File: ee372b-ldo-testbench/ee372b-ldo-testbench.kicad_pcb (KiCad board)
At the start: 4 copper layers, 118 parts, among them J1 PEC02SAAN, J10 OUT_S, J11 VOUT, J12 VDD_BUF, J13 V_SIG, J14 PEC03SAAN, J15 VSIG_BUF, J16 PEC03SAAN, J17 PEC03SAAN, J18 PEC03SAAN, J19 PEC03SAAN, J2 PEC02SAAN, J20 VREF_EXTERNAL, J21 PEC02SAAN, J22 PEC02SAAN, J23 PEC02SAAN, J24 PEC02SAAN, J25 PEC03SAAN, J3 GND, J4 1V8, J5 3v3_EXTERNAL, J9 IN_S, Q1 FDV305N, Q2 FDV305N, Q3 FDV305N, Q4 FDV305N, Q5 FDV305N, U1 MMSZ4679T1G, U3 ADS1220IPW, U4 BUF634AIDR

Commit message: omg fit everything in 100x100
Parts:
- added R64: 0, Resistor_SMD:R_0805_2012Metric_Pad1.20x1.40mm_HandSolder, F.Cu at (169.8, 50.4)
- added R65: 0, Resistor_SMD:R_0805_2012Metric_Pad1.20x1.40mm_HandSolder, F.Cu at (172.8, 50.4)
- moved C16 96.8 mm to (162.7, 68.1), turned to -90 degrees
- moved C14 96.5 mm to (173.4, 68.2), turned to -90 degrees
- moved C15 96.5 mm to (168.0, 68.1), turned to -90 degrees
- moved C2 88.7 mm to (175.7, 58.2)
- moved C1 88.7 mm to (175.7, 62.1)
- moved C8 88.7 mm to (177.7, 58.2)
- moved C12 88.7 mm to (177.7, 62.1)
- moved J25 88.2 mm to (162.1, 49.5), turned to -90 degrees
- moved U3 87.4 mm to (169.7, 61.2)
- moved R6 86.4 mm to (175.5, 68.2), turned to 90 degrees
- moved R1 85.2 mm to (162.9, 60.5)
- moved R2 85.2 mm to (162.9, 58.4)
- moved R5 84.9 mm to (181.8, 57.3), turned to 180 degrees
- moved R44 83.7 mm to (166.6, 50.4)
- moved R8 83.5 mm to (164.8, 68.2), turned to 90 degrees
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
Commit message: re add caps for each pin
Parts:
- removed C27: 100nF, Capacitor_SMD:C_0805_2012Metric_Pad1.18x1.45mm_HandSolder
- added C24: 100nF, Capacitor_SMD:C_0805_2012Metric_Pad1.18x1.45mm_HandSolder, F.Cu at (198.7, 37.3)
- added C29: 100nF, Capacitor_SMD:C_0805_2012Metric_Pad1.18x1.45mm_HandSolder, F.Cu at (201.4, 49.3)
- added C30: 100nF, Capacitor_SMD:C_0805_2012Metric_Pad1.18x1.45mm_HandSolder, F.Cu at (206.9, 40.1)
- moved J3 15.1 mm to (145.2, 76.7)
- moved J5 15.0 mm to (145.2, 91.8)
- moved R37 1.74 mm to (202.9, 24.1)
- moved R48 1.29 mm to (199.8, 56.6)
- moved R49 1.29 mm to (207.3, 56.6)
- moved R58 1.29 mm to (204.8, 56.6)
- moved R60 1.29 mm to (201.8, 56.6)
- moved C7 1.14 mm to (203.5, 49.3)
- moved J25 0.15 mm to (162.2, 49.6)
- turned C23 to -90 degrees
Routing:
- net Net-(C10-Pad2): track 0.00 -> 1.48 mm

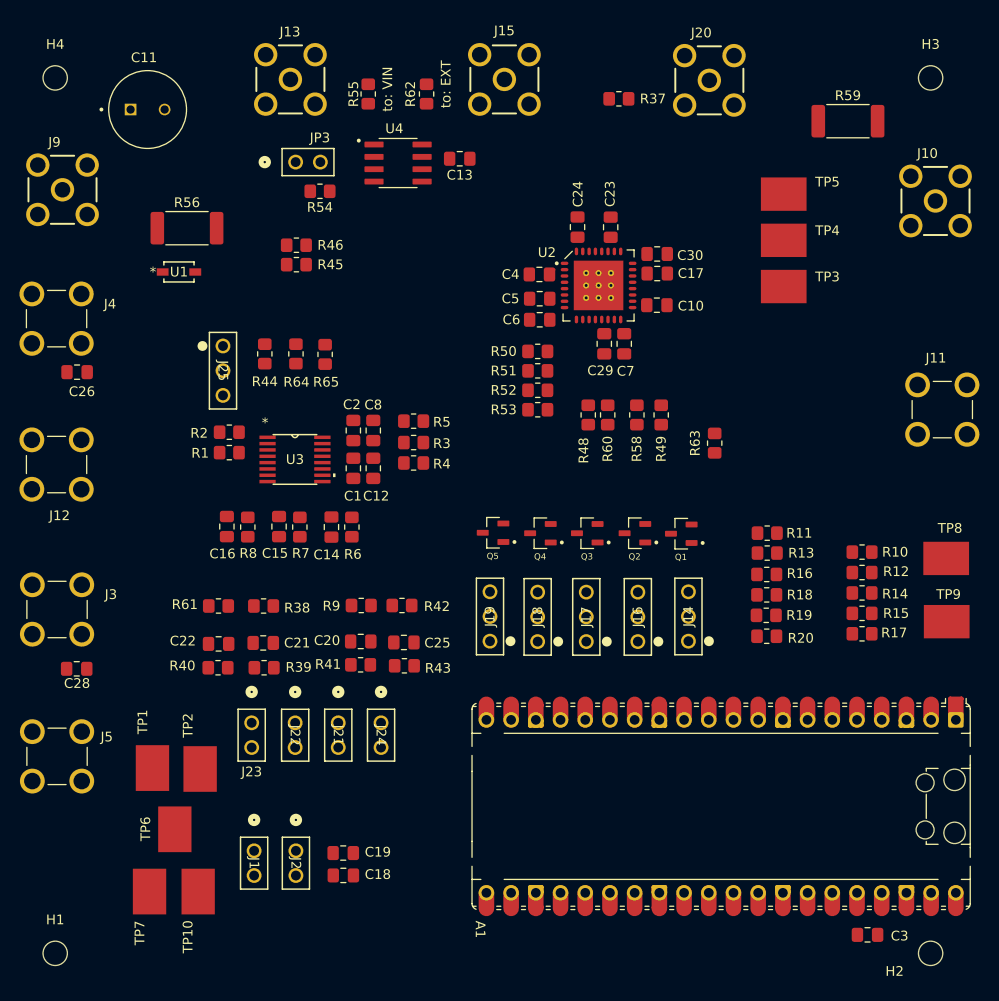
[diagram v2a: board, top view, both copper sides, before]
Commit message: added more GND test points and EP to VSS r0 thing
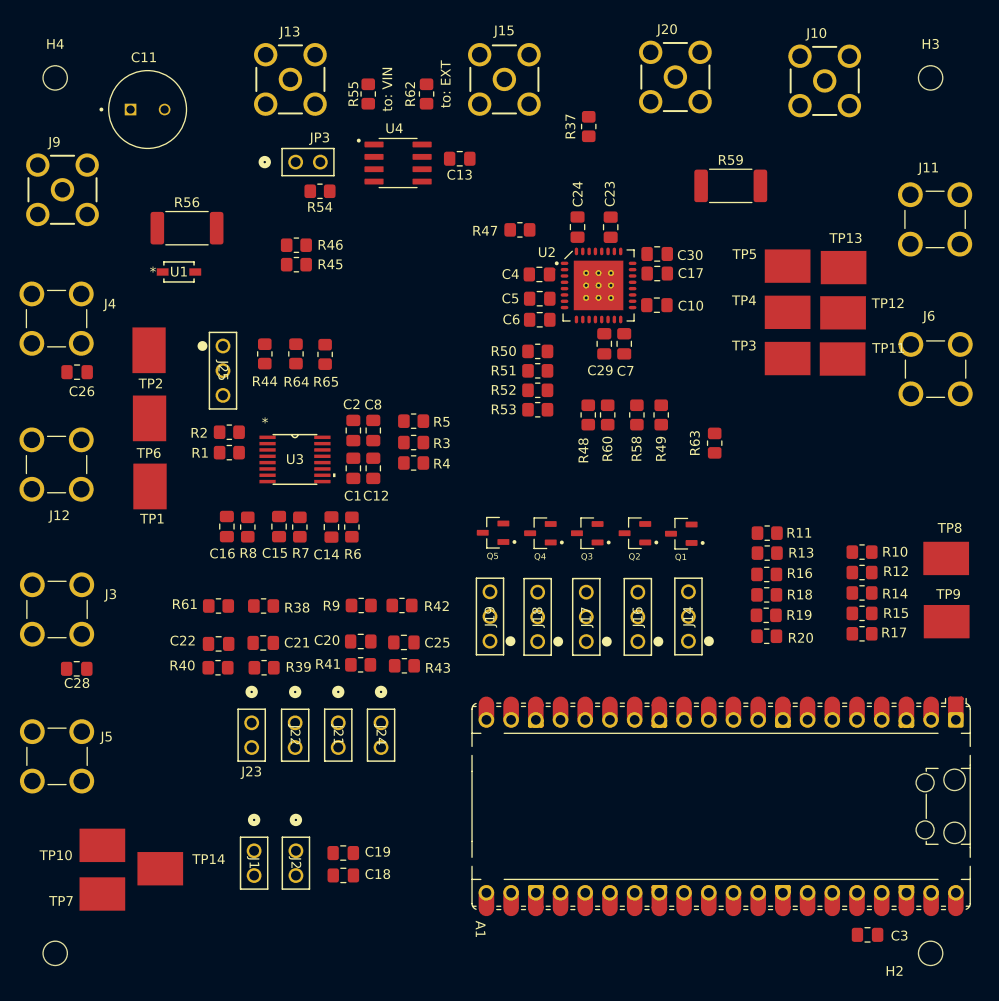
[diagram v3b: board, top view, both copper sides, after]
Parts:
- added J6: GND, 1_EE372_DemoBoard:CALTEST_CT3151-2, F.Cu at (235.5, 51.9)
- added R47: 0, Resistor_SMD:R_0805_2012Metric_Pad1.20x1.40mm_HandSolder, F.Cu at (192.8, 37.6)
- added TP11: GND, 1_EE372_DemoBoard:KEYSTONE_5016, F.Cu at (225.9, 50.9)
- added TP12: GND, 1_EE372_DemoBoard:KEYSTONE_5016, F.Cu at (226.0, 46.1)
- added TP13: GND, 1_EE372_DemoBoard:KEYSTONE_5016, F.Cu at (226.1, 41.5)
- added TP14: GND, 1_EE372_DemoBoard:KEYSTONE_5016, F.Cu at (155.8, 103.3)
- moved TP2 43.4 mm to (154.7, 50.0), turned to -90 degrees
- moved TP6 42.3 mm to (154.7, 57.0), turned to -90 degrees
- moved TP1 29.0 mm to (154.8, 64.0), turned to -90 degrees
- moved J11 19.6 mm to (235.5, 36.5)
- moved J10 16.8 mm to (224.1, 22.3)
- moved R59 13.8 mm to (214.4, 33.1)
- moved TP10 10.9 mm to (149.8, 100.9), turned to 180 degrees
- moved TP3 7.41 mm to (220.3, 50.9)
- moved TP4 7.41 mm to (220.3, 46.1)
- moved TP5 7.41 mm to (220.3, 41.4)
- moved TP7 4.86 mm to (149.8, 105.9), turned to 180 degrees
- moved R37 4.21 mm to (199.8, 27.0), turned to -90 degrees
- moved J20 3.51 mm to (208.8, 21.9)
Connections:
- U2 pad 33: unconnected-(U2-EP-Pad33)_8 -> Net-(U2-EP)

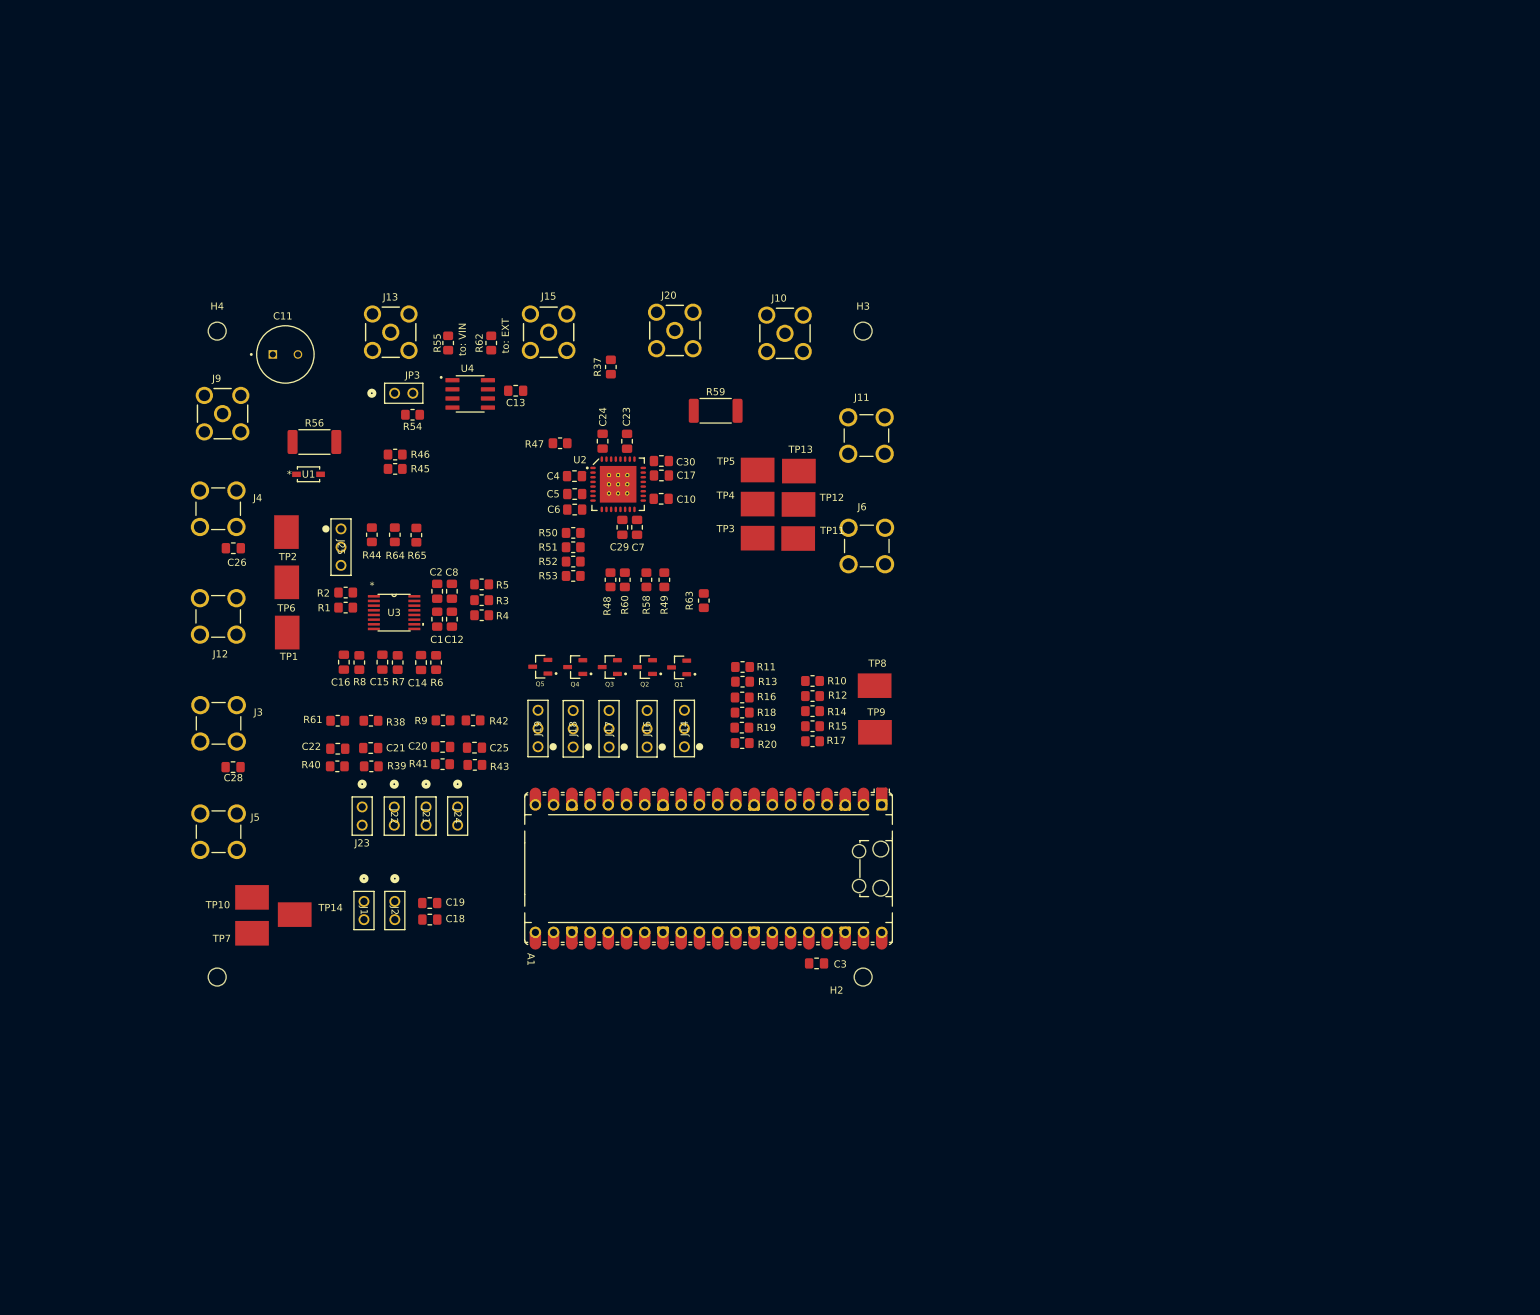
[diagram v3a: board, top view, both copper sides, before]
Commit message: first plane fill on L2 GND
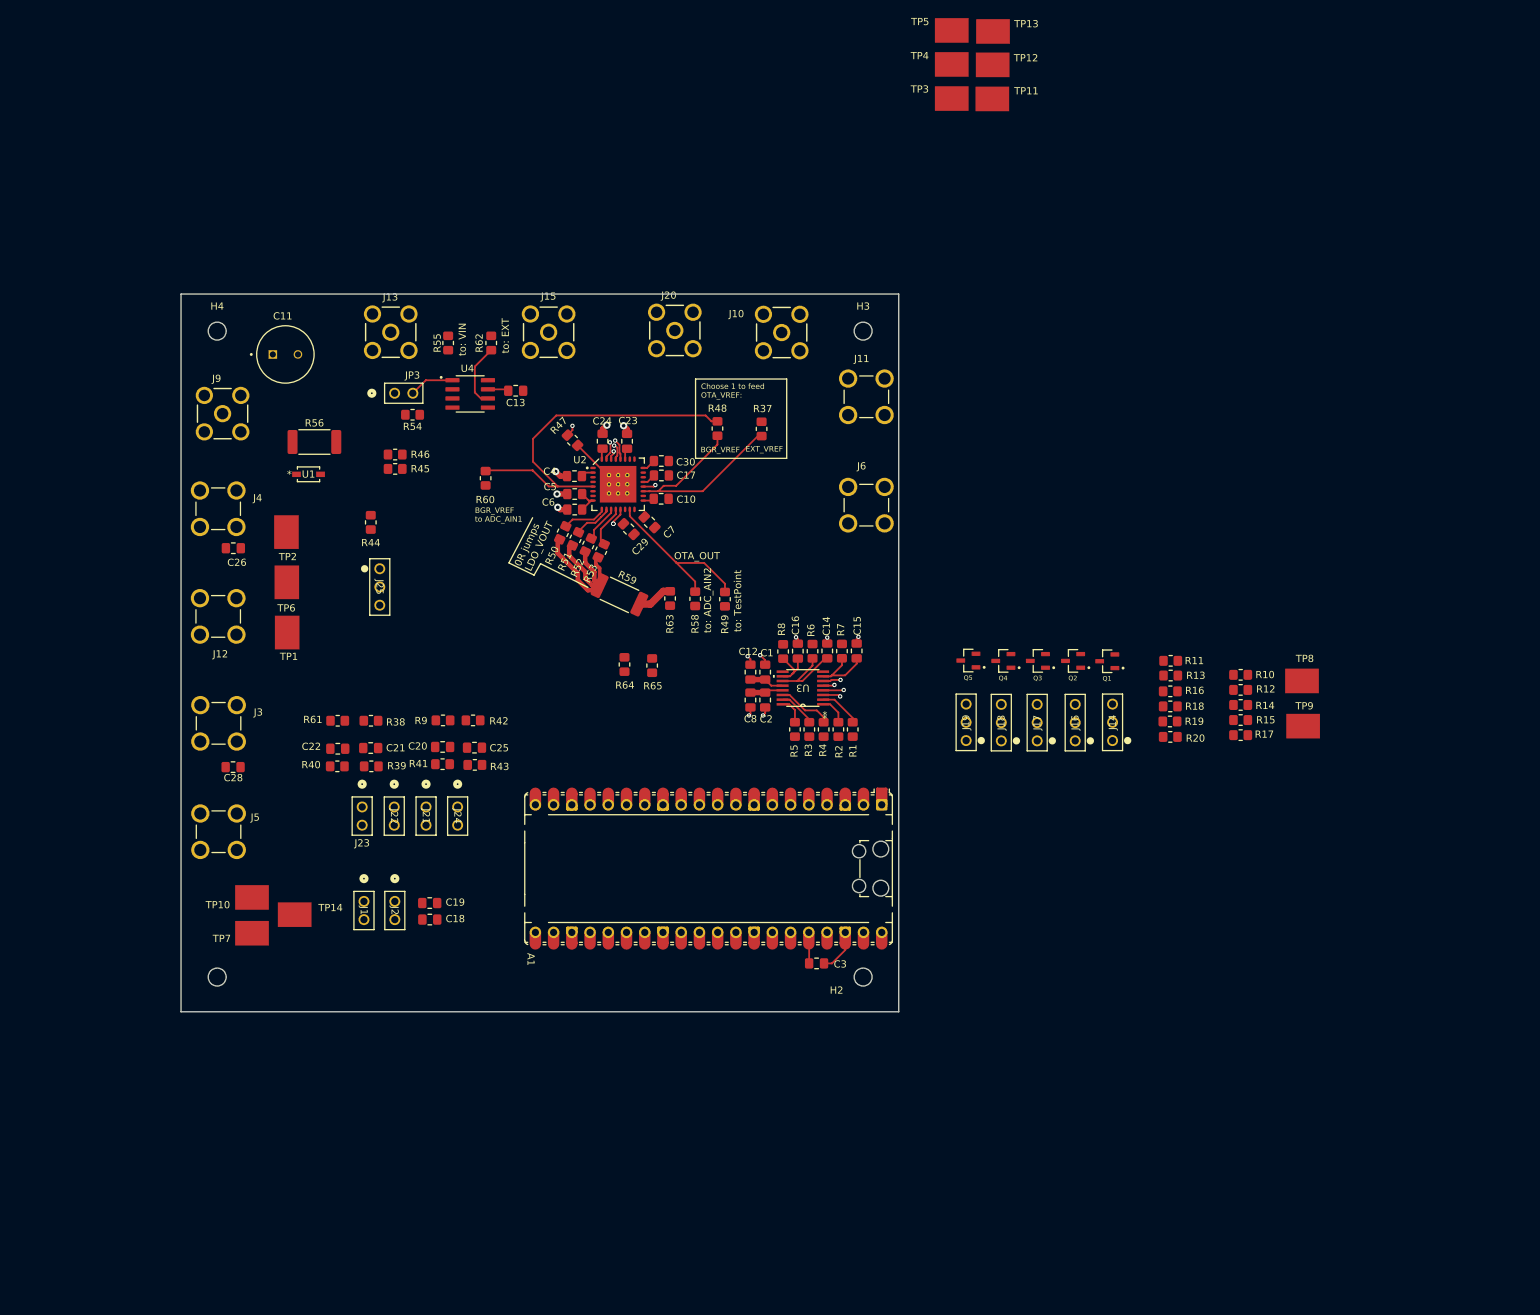
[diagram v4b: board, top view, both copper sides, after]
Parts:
- moved R1 72.7 mm to (233.6, 77.5), turned to -90 degrees
- moved R2 71.3 mm to (231.6, 77.5), turned to 90 degrees
- moved TP11 67.0 mm to (253.0, -10.3)
- moved TP12 67.0 mm to (253.1, -15.1)
- moved TP13 67.0 mm to (253.1, -19.8)
- moved TP3 67.0 mm to (247.3, -10.4)
- moved TP4 67.0 mm to (247.3, -15.2)
- moved TP5 67.0 mm to (247.3, -19.9)
- moved C15 66.1 mm to (234.1, 66.6), turned to 90 degrees
- moved C16 63.3 mm to (225.9, 66.6), turned to 90 degrees
- moved R7 61.9 mm to (232.1, 66.6), turned to -90 degrees
- moved Q3 59.7 mm to (259.4, 68.0)
- moved R10 59.7 mm to (287.6, 69.9)
- moved R11 59.7 mm to (277.9, 67.9)
- moved R12 59.7 mm to (287.6, 72.0)
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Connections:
- R47 pad 1: /VSS -> GND
- U3 pad 6: /LDO_GND -> /AIN3_LDO_GND
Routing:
- net Net-(U2-BGR_VREF): track 0.00 -> 51.3 mm
- net GND: track 0.00 -> 38.4 mm, vias 0 -> 23
- net /BGR_VREF: track 0.00 -> 31.3 mm
- net /LDO_VOUT: track 0.00 -> 28.9 mm
- net Net-(U2-OTA_OUT): track 0.00 -> 24.5 mm
- net Net-(C10-Pad2): track 1.48 -> 14.5 mm
- net /AIN0_ADC: track 0.00 -> 11.6 mm
- net /3V3: track 0.00 -> 9.44 mm
- net /AIN2_ADC: track 0.00 -> 9.31 mm
- net /VSIG_BUF: track 0.00 -> 9.01 mm
- net Net-(U3-*DRDY): track 0.00 -> 7.70 mm
- net /AIN1_ADC: track 0.00 -> 6.81 mm
- net Net-(U4-BW): track 0.00 -> 6.27 mm
- net Net-(R50-Pad2): track 0.00 -> 6.19 mm
- net Net-(U2-EP): track 0.00 -> 6.09 mm
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- added copper zone on In1.Cu, net GND
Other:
- board outline added: 100 x 100 mm
- board text added: "0R jumps LDO_VOUT"
- board text added: "BGR_VREF"
- board text added: "BGR_VREF to ADC_AIN1"
- board text added: "Choose 1 to feed OTA_VREF:"
- board text added: "EXT_VREF"
- board text added: "OTA_OUT"
- board text added: "to: ADC_AIN2"
- board text added: "to: TestPoint"

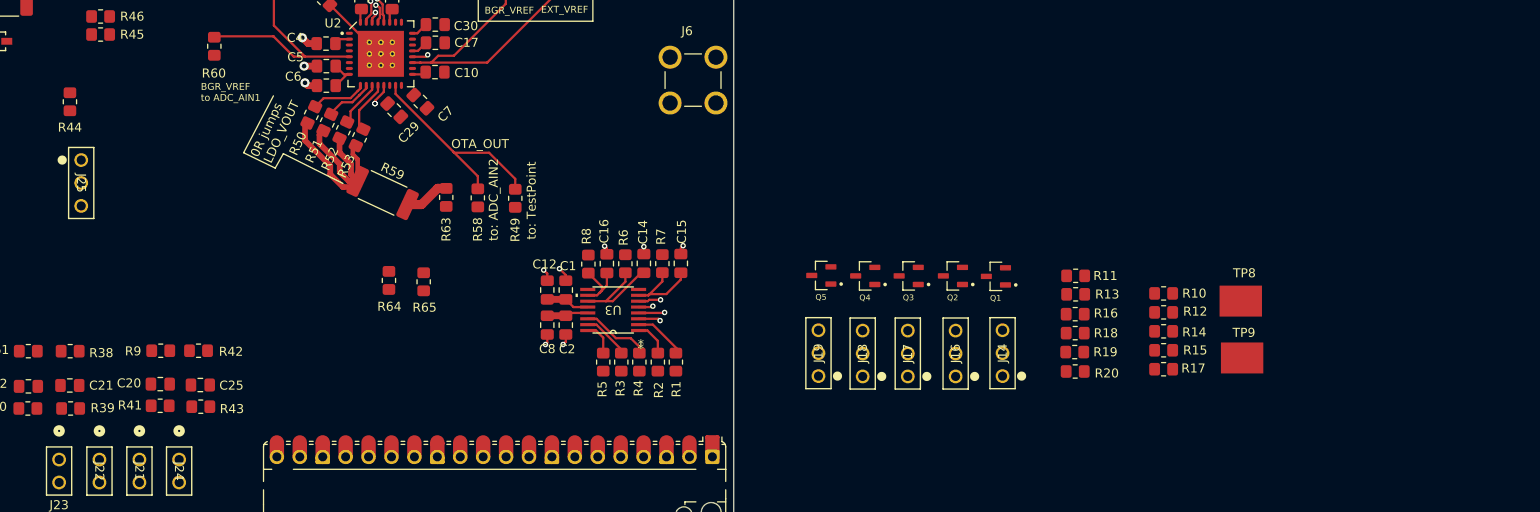
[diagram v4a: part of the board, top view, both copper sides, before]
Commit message: connected ADC PICO
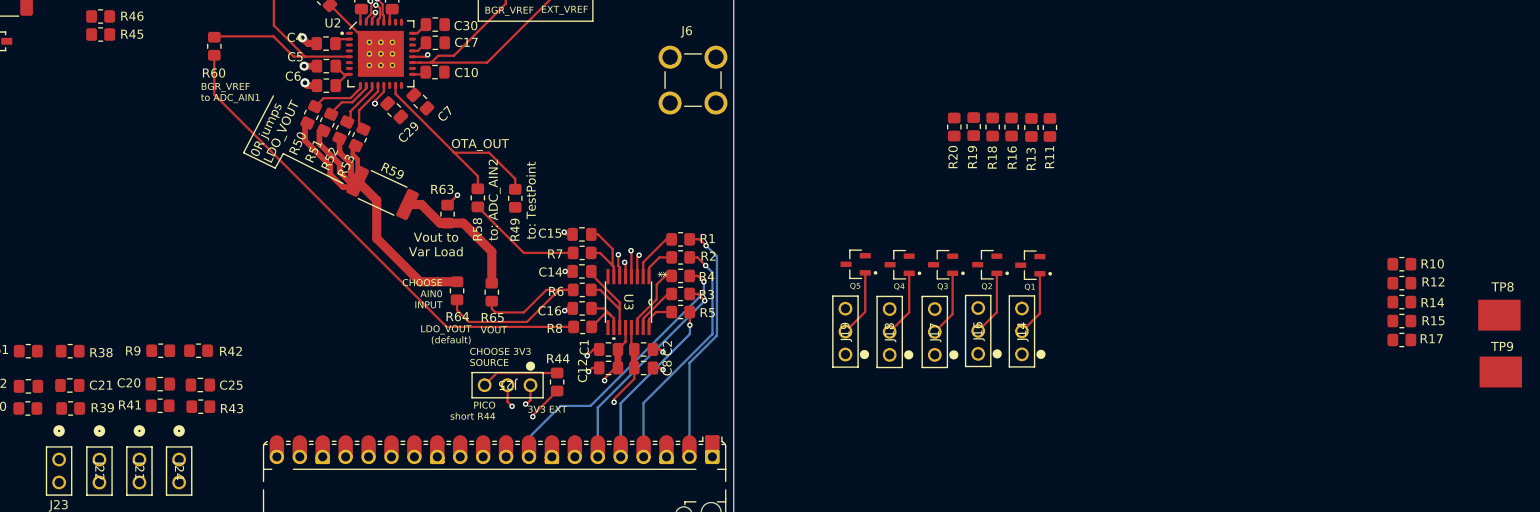
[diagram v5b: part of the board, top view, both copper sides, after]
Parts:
- moved R44 62.3 mm to (220.4, 79.7), turned to -90 degrees
- moved J25 55.7 mm to (217.4, 80.1), turned to 180 degrees
- moved R20 30.2 mm to (264.4, 51.5), turned to -90 degrees
- moved TP8 28.7 mm to (324.8, 72.3)
- moved TP9 28.7 mm to (325.0, 78.6)
- moved R19 27.4 mm to (266.6, 51.4), turned to -90 degrees
- moved R10 26.6 mm to (314.0, 66.7)
- moved R12 26.6 mm to (314.0, 68.8)
- moved R14 26.6 mm to (314.0, 70.8)
- moved R15 26.6 mm to (314.0, 73.0)
- moved R17 26.6 mm to (314.0, 75.0)
- moved R18 24.6 mm to (268.6, 51.5), turned to -90 degrees
- moved R16 21.9 mm to (270.8, 51.5), turned to -90 degrees
- moved R13 19.1 mm to (272.9, 51.5), turned to -90 degrees
- moved R11 16.7 mm to (275.0, 51.5), turned to -90 degrees
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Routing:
- net /AIN1_SIGNAL: track 0.00 -> 54.8 mm
- net /3V3: track 9.44 -> 42.0 mm, vias 0 -> 3
- net /3V3_PICO: track 3.54 -> 35.0 mm, vias 0 -> 1
- net /pico_irq: track 0.00 -> 31.2 mm, vias 0 -> 1
- net /pico_spi_cs: track 0.00 -> 27.3 mm, vias 0 -> 1
- net /AIN0_SIGNAL: track 0.00 -> 27.1 mm
- net /pico_spi_clk: track 0.00 -> 26.8 mm, vias 0 -> 1
- net /pico_spi_rx: track 0.00 -> 24.2 mm, vias 0 -> 1
- net /LDO_VOUT: track 28.9 -> 48.2 mm
- net /pico_spi_tx: track 0.00 -> 19.2 mm, vias 0 -> 1
- net /AIN2_SIGNAL: track 0.00 -> 12.7 mm
- net /VOUT: track 5.03 -> 14.2 mm
- net Net-(J25-Pad3): track 0.00 -> 8.59 mm
- net /VG4: track 0.00 -> 7.42 mm
- net /VG3: track 0.00 -> 7.40 mm
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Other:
- board text added: "3V3 EXT"
- board text added: "CHOOSE 3V3 SOURCE"
- board text added: "CHOOSE AIN0 INPUT"
- board text added: "LDO_VOUT (default)"
- board text added: "PICO short R44"
- board text added: "VOUT"
- board text added: "Vout to Var Load"
